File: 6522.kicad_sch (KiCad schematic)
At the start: 37 parts, among them J7 AUDIO_OUT, P1 A2Bus, U1 AY-3-8910, U2 6522, U3 74LS05, U4 AY-3-8910, U5 6522

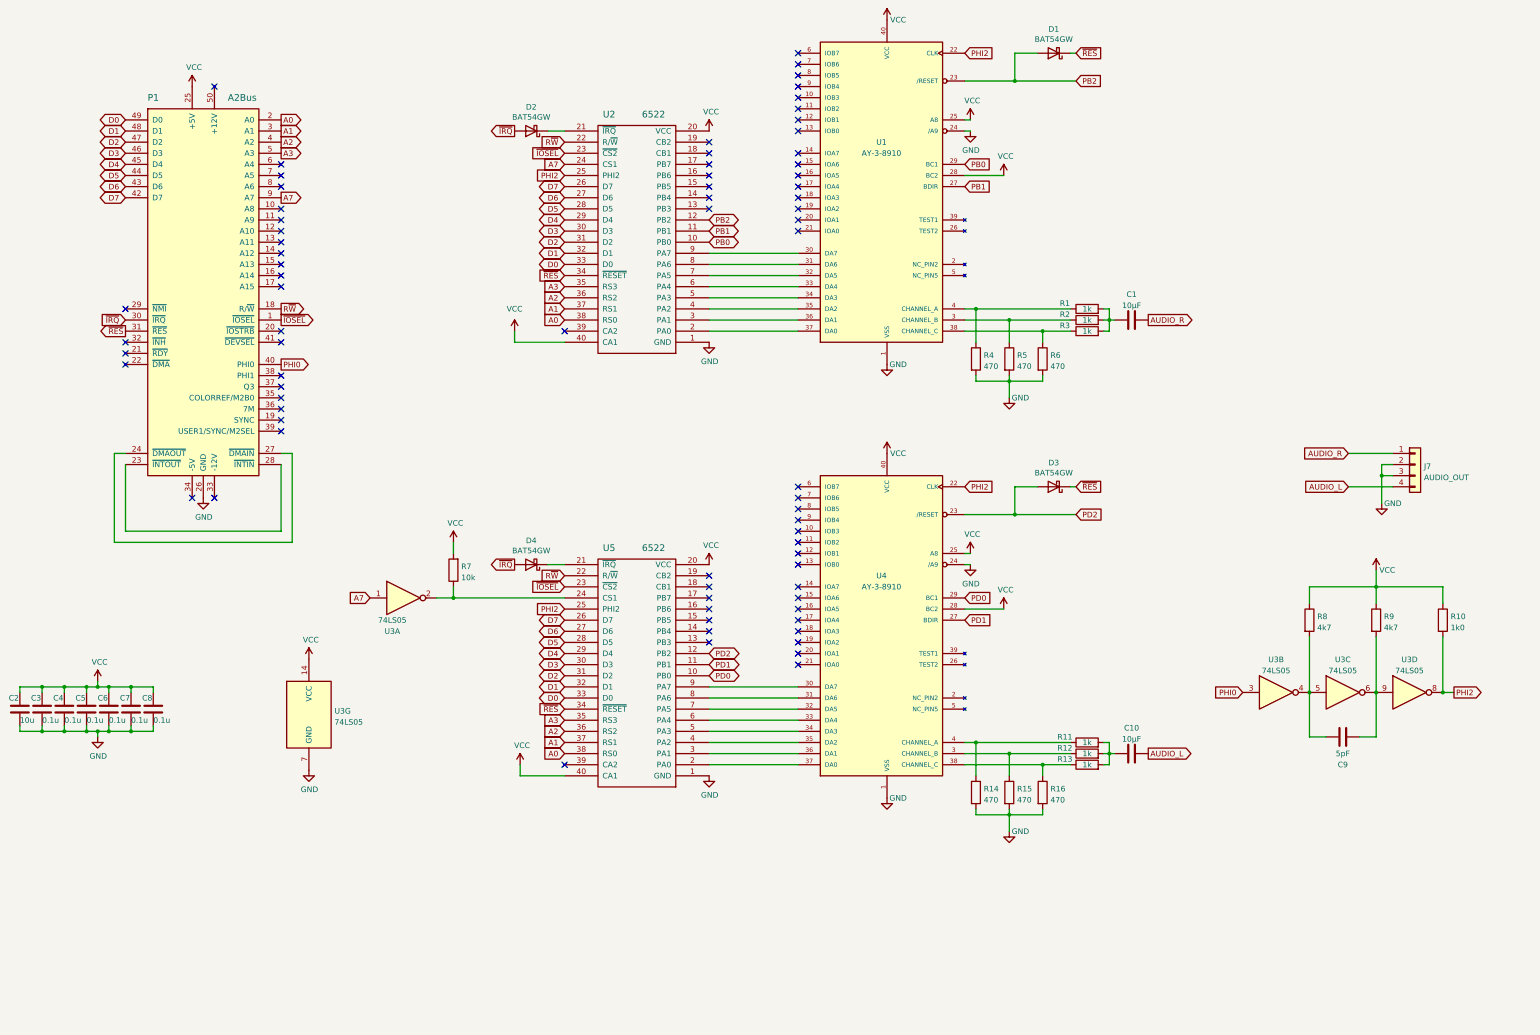
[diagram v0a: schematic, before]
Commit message: All-SMD version
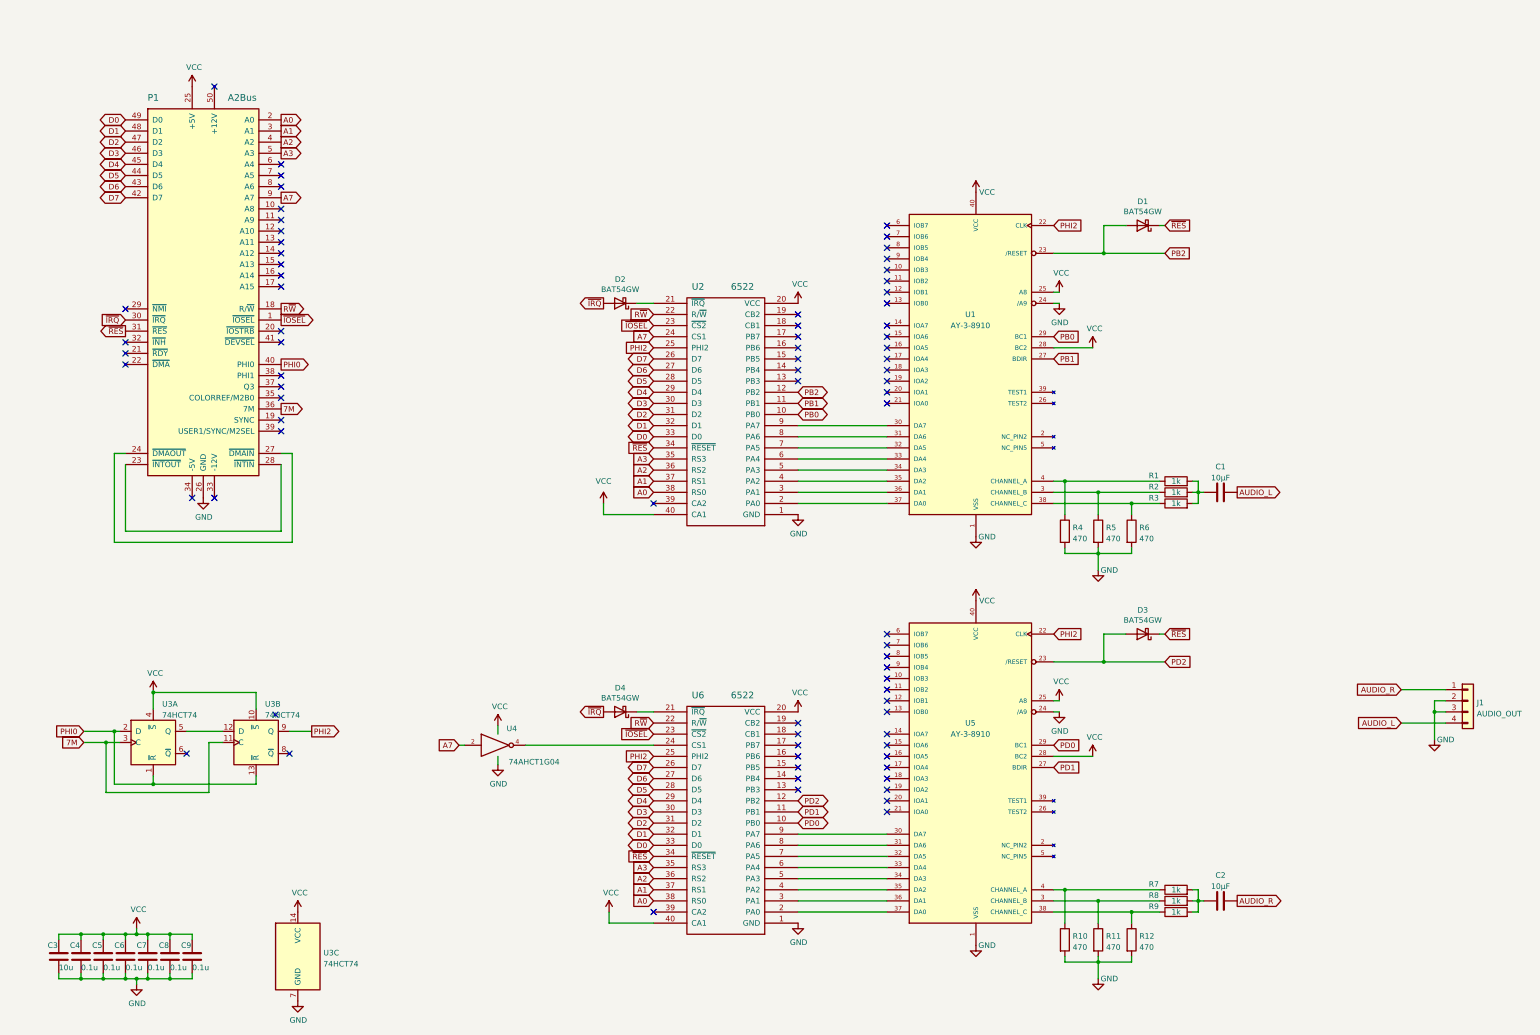
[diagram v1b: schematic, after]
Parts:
- removed C9: 5pF, Capacitor_SMD:C_0805_2012Metric, symbol Device:C
- removed R10: 1k0, Resistor_SMD:R_0805_2012Metric, symbol Device:R
- removed R7: 10k, Resistor_SMD:R_0805_2012Metric, symbol Device:R
- removed R8, R9: 4k7, Resistor_SMD:R_0805_2012Metric, symbol Device:R
- removed U3: 74LS05, Package_DIP:DIP-14_W7.62mm, symbol 74xx:74LS05
- added U3: 74HCT74, Package_SO:TSSOP-14_4.4x5mm_P0.65mm, symbol 74xx:74LS74
- added U4: 74AHCT1G04, 74ahct1g04:74AHCT1G04W5-7, symbol 74xGxx:74AHCT1G04
- renumbered C10 to C2, C2 to C3, C3 to C4, C4 to C5, C5 to C6, C6 to C7, C7 to C8, C8 to C9, J7 to J1, R14 to R10, R15 to R11, R16 to R12, R11 to R7, R12 to R8, R13 to R9, U4 to U5, U5 to U6
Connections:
- net A7: now also U4.2
- net AUDIO_L: now also C1.2; no longer C2.2
- net AUDIO_R: now also C2.2; no longer C1.2
- net GND: now also U3.7 (GND), U4.3 (GND)
- net PHI0: now also U3.1 (~{R}), U3.13 (~{R}), U3.2 (D)
- net PHI2: now also U3.9 (Q)
- net VCC: now also U3.10 (~{S}), U3.14 (VCC), U3.4 (~{S}), U4.5 (VCC)
- net 7M: now reaches P1.36 (7M)
- net 7M: now also U3.11 (C), U3.3 (C)
- net at U6.24 (CS1): now also U4.4
- new net: U3.12 (D), U3.5 (Q)
- no-connect marks 74 -> 76
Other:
- moved on the sheet: C1, C2, C3, C4, C5, C6, C7, C8, C9, D1, D2, D3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
